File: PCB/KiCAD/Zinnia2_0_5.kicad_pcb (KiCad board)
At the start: 2 copper layers, 125.4 x 90.3 mm, 112 parts, among them J1 Conn_01x06_Female, J11 Conn_01x02, J14 Conn_01x06, J15 Conn_01x06, J2 Conn_01x02, J4 Conn_01x01, J5 Rumble, J6 PinSocket_1x04_P2.00mm_Vertic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, J9 USB_B_Micro, Q1 Q_NMOS_GSD, Q2 Q_PMOS_GDS, Q3 Q_NMOS_GSD, SW1 A, SW10 Dup, SW11 Dright, SW12 Ddown, SW2 B, SW3 X, SW4 Y, SW5 Start, SW6 L, SW7 R, SW8 Z, SW8L ZL, SW9 Dleft, U1 MCP3002, U10 DRV5055A2xDBZxQ1, U11 DRV5055A2xDBZxQ1, U12 USBLC6-2P6, U13 USBLC6-2P6, U2 Stickbox_Assembly_Main, U3 MCP3002, U4 DRV5055A2xDBZxQ1, U5 Stickbox_Assembly_CStick, U6 AMS1117-3.3, U7 W25Q128JVS, U8 RP2040, U9 DRV5055A2xDBZxQ1, Y1 Crystal_GND24

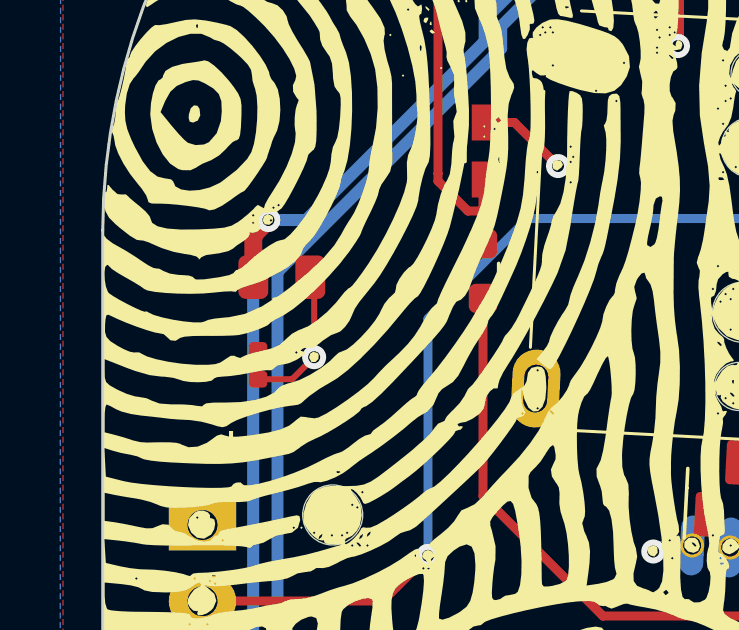
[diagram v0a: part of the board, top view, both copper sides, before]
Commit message: Added Silkscreen variant
Added flower variant silkscreen
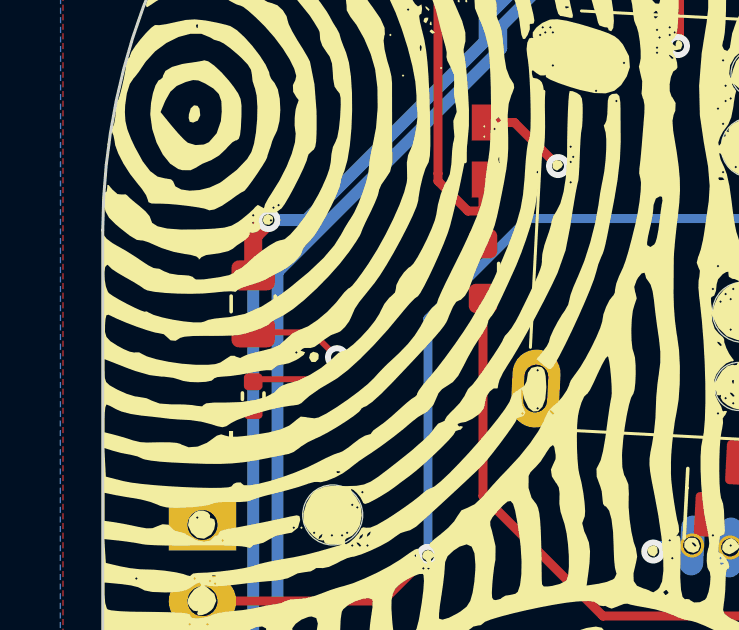
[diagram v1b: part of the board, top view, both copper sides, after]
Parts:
- moved C16 1.30 mm to (53.3, 53.6), turned to -90 degrees
- moved C29 1.06 mm to (53.3, 56.7), turned to 90 degrees
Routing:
- net GND: track 161.4 -> 162.6 mm

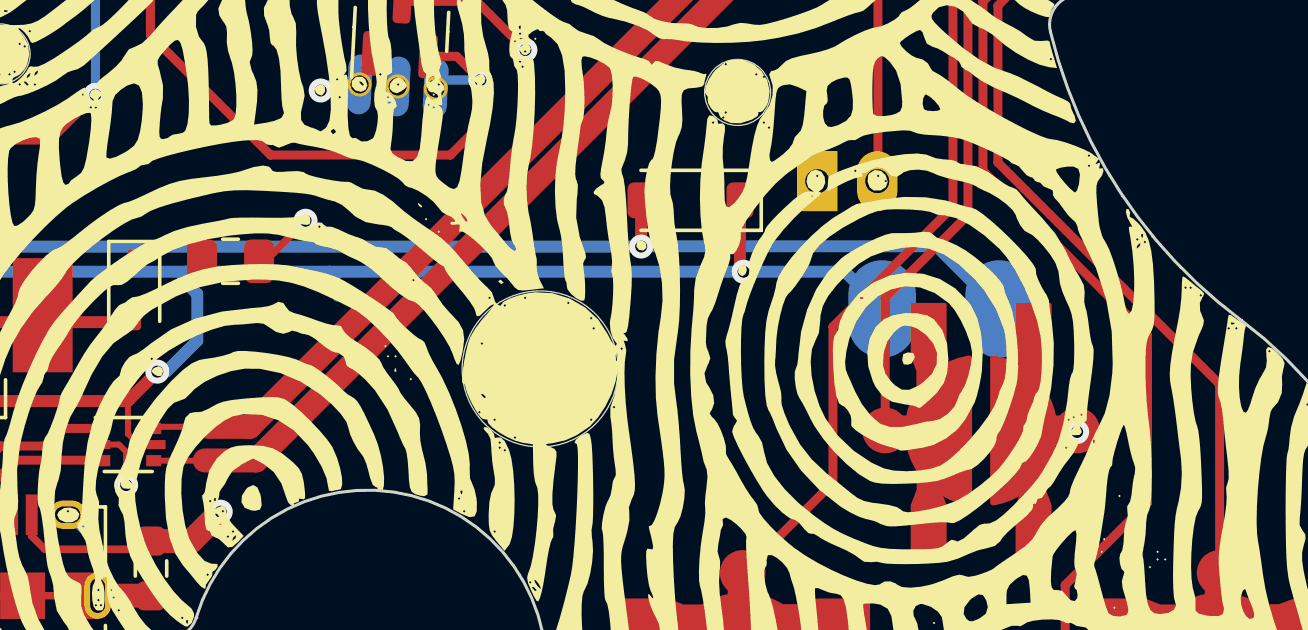
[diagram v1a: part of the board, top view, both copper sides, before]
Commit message: added 3.3v pad on back
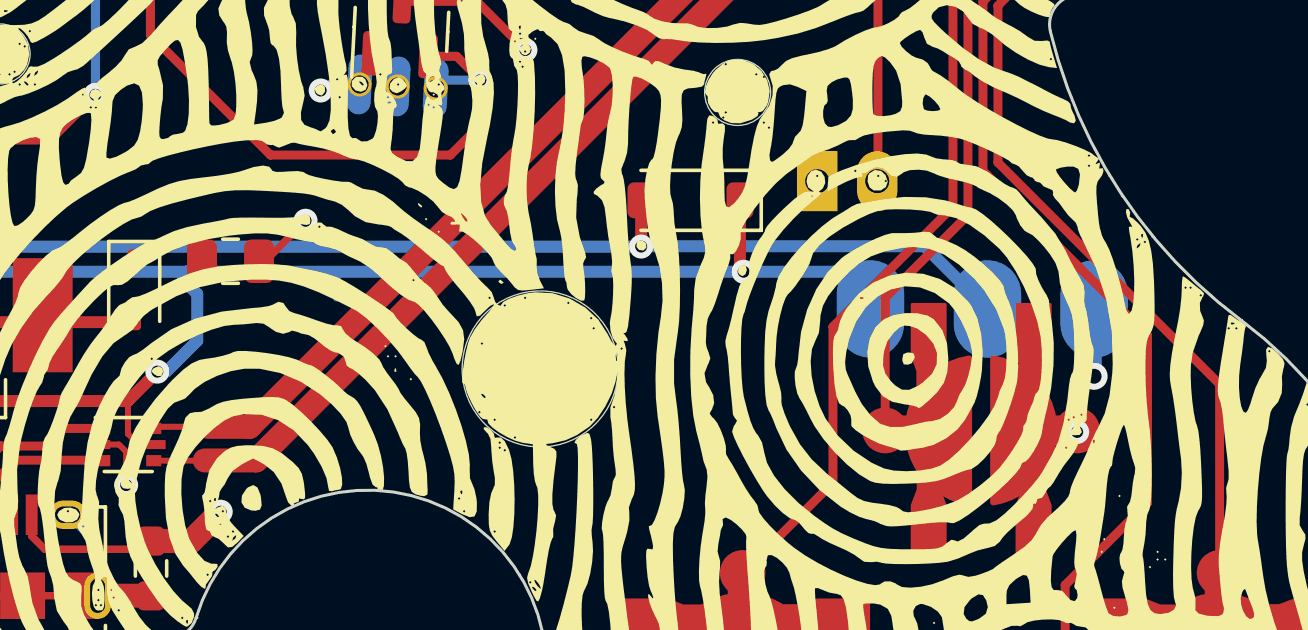
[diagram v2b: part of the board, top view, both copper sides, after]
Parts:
- added ?: , , F.Cu at (92.5, 69.3)
- moved J5 0.39 mm to (85.8, 69.1)
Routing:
- net +3V3: track 72.6 -> 74.9 mm, vias 16 -> 17
